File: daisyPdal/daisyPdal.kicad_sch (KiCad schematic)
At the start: 17 parts, among them J1 AudioJack2, U1 L78L05_TO92, U2 TL072

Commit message: Get the input and output buffers on the schematic
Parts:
- added C10, C9: 1u, symbol Device:C
- added J2: AudioJack2, symbol Connector_Audio:AudioJack2
- added R5, R6: 1M, symbol Device:R_US
- added R7: 100K, symbol Device:R_US
- added R8: 100R, symbol Device:R_US
- C6: value C -> 100p
- C7: value C -> 1n
- C8: value C -> 1u
- R1, R2: value R_US -> 1M
- R3: value R_US -> 1k
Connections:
- net +5V: now also R5.1
- net GND: now also A1.20 (AGND), A1.40 (DGND), J2.S, R6.2, R7.2
- net Left in: now also A1.16 (AUDIO_IN_1)
- net VCC: now also A1.39 (VIN)
- net Left out: now reaches A1.18 (AUDIO_OUT_1)
- net Left out: now also C10.1
- net at U2.5 (+): now also C10.2, R5.2, R6.1
- net at U2.6 (-): now also U2.7, R8.1
- new net: C9.1, R8.2
- new net: C9.2, J2.T, R7.1
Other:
- moved on the sheet: U2B

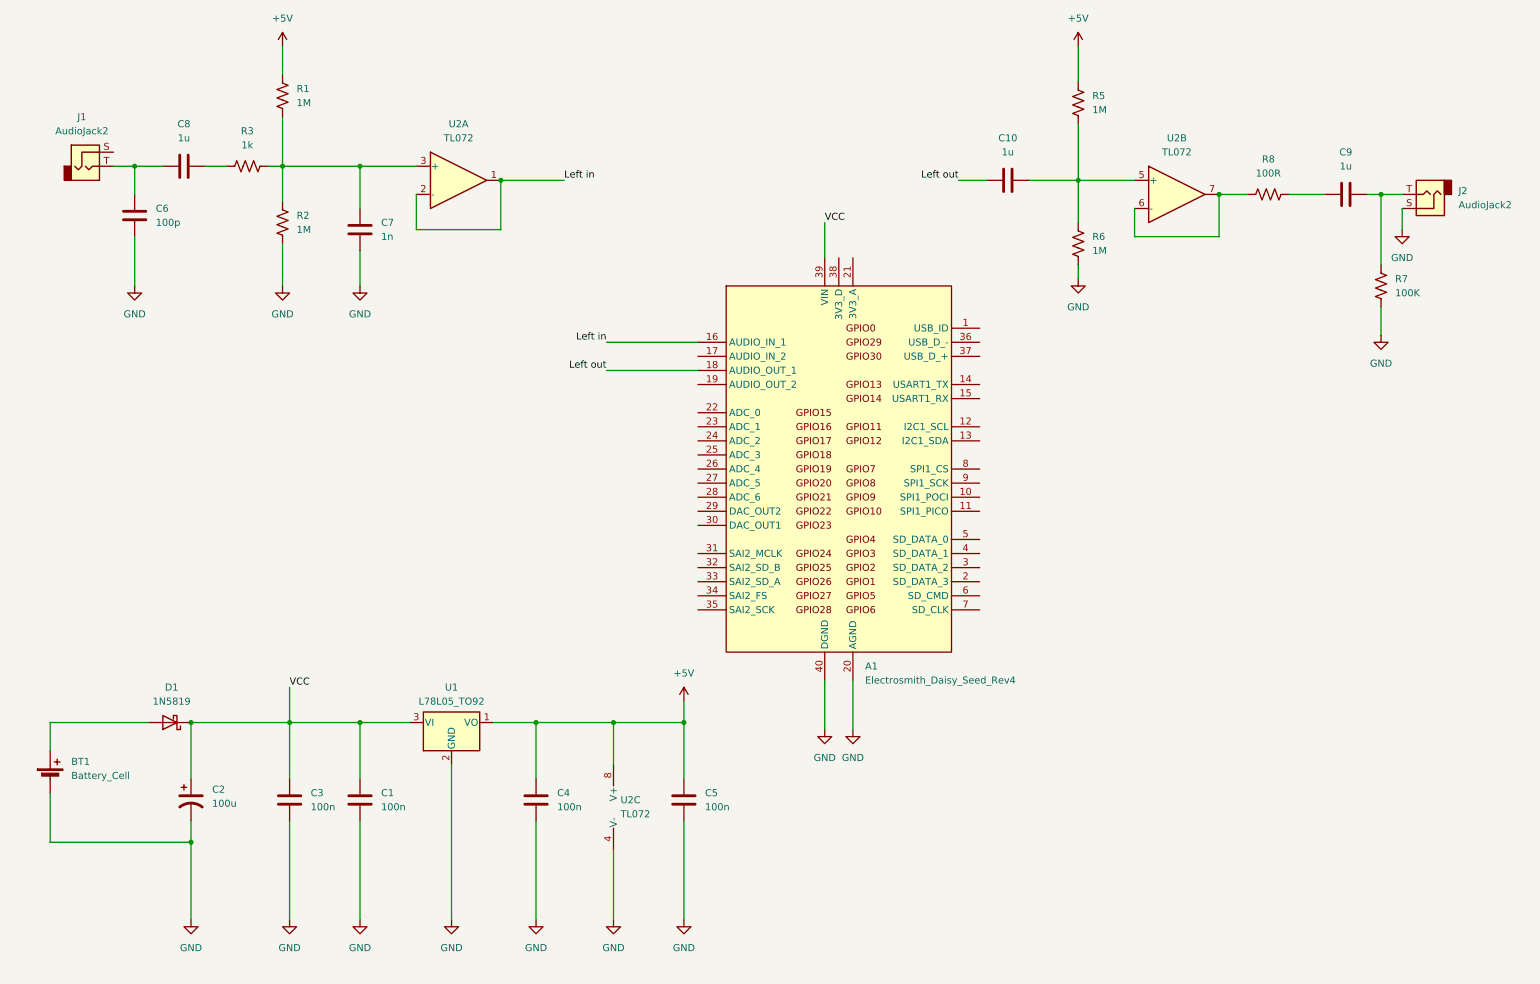
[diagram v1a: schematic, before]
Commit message: Update schematic with pots, switches, encoder, LEDs
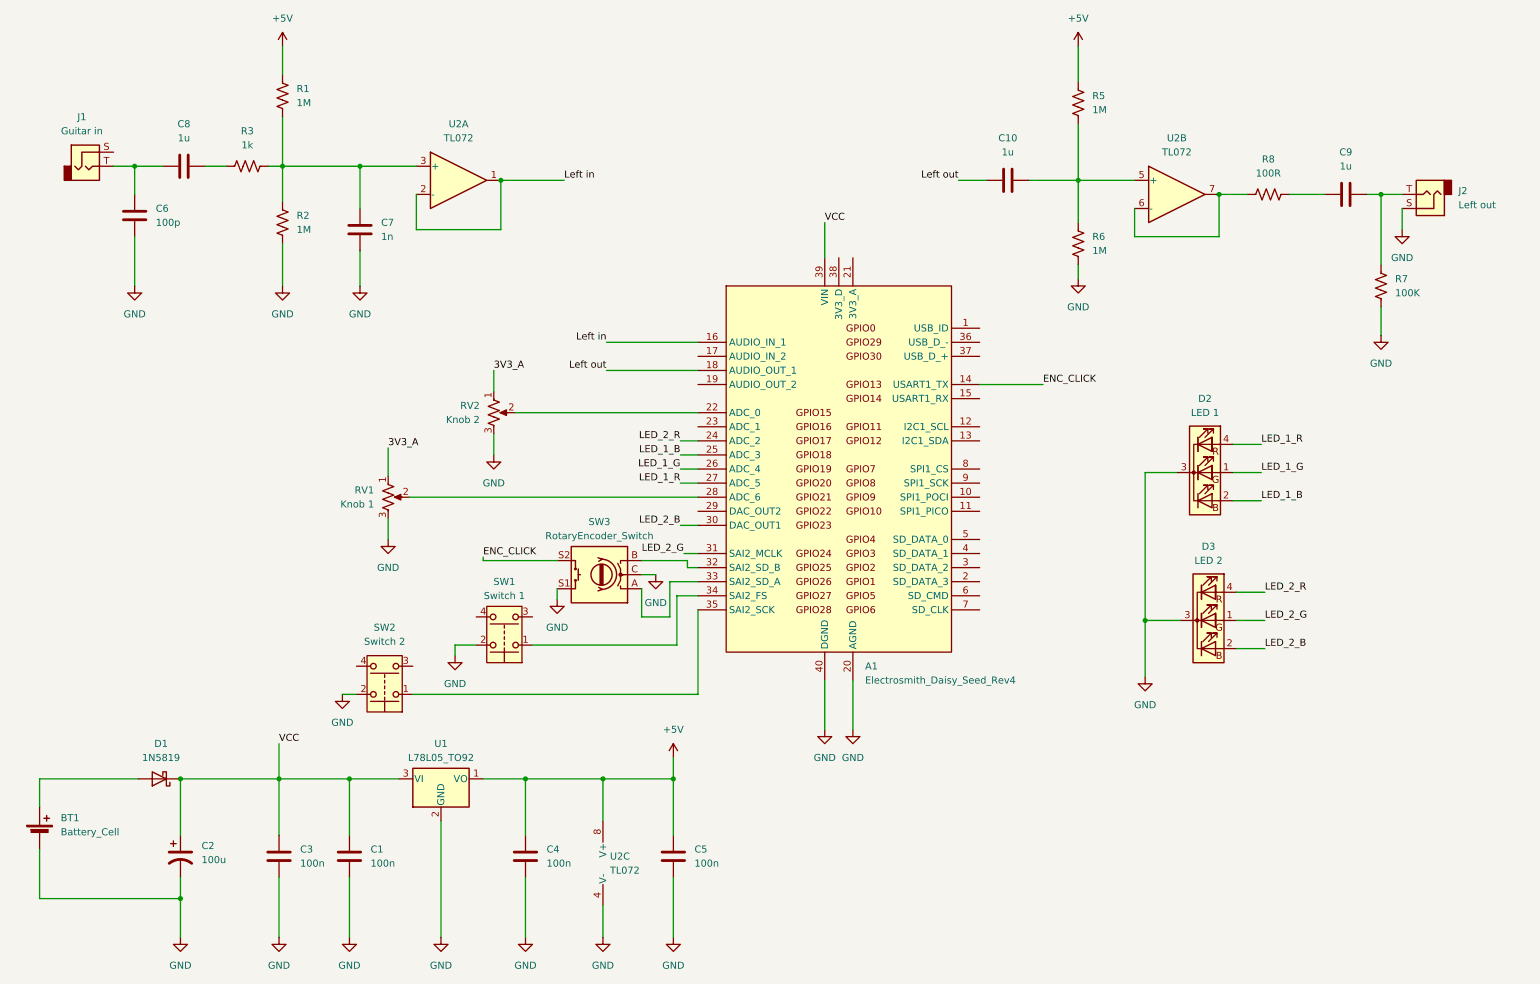
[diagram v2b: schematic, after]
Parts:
- added D2: LED 1, symbol Device:LED_GBKR
- added D3: LED 2, symbol Device:LED_GBKR
- added RV1: Knob 1, symbol Device:R_Potentiometer_US
- added RV2: Knob 2, symbol Device:R_Potentiometer_US
- added SW1: Switch 1, symbol Switch:SW_Push_Dual
- added SW2: Switch 2, symbol Switch:SW_Push_Dual
- added SW3: RotaryEncoder_Switch, symbol Device:RotaryEncoder_Switch
- BT1: footprint (none) -> Jumper:SolderJumper-2_P1.3mm_Open_RoundedPad1.0x1.5mm
- C1, C2, C3, C4, C5, C6: footprint (none) -> Capacitor_THT:CP_Radial_D8.0mm_P3.80mm
- C10, C7, C8, C9: footprint (none) -> Capacitor_THT:C_Rect_L7.0mm_W2.0mm_P5.00mm
- J1: value AudioJack2 -> Guitar in; footprint (none) -> Connector_Audio:Jack_6.35mm_Neutrik_NRJ4HF_Horizontal
- J2: value AudioJack2 -> Left out; footprint (none) -> Connector_Audio:Jack_6.35mm_Neutrik_NRJ4HF_Horizontal
- R1, R2, R3, R5, R6, R7, R8: footprint (none) -> Resistor_THT:R_Box_L13.0mm_W4.0mm_P9.00mm
- U2: footprint (none) -> Package_DIP:DIP-8_W7.62mm_Socket
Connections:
- net GND: now also D2.3 (K), D3.3 (K), RV1.3, RV2.3, SW1.2, SW2.2, SW3.C, SW3.S1
- net ENC_CLICK: now reaches A1.14 (USART1_TX)
- net ENC_CLICK: now also SW3.S2
- net at A1.22 (ADC_0): now also RV2.2
- net LED_2_R: now reaches A1.24 (ADC_2)
- net LED_2_R: now also D3.4 (RA)
- net LED_1_B: now reaches A1.25 (ADC_3)
- net LED_1_B: now also D2.2 (BA)
- net LED_1_G: now reaches A1.26 (ADC_4)
- net LED_1_G: now also D2.1 (GA)
- net LED_1_R: now reaches A1.27 (ADC_5)
- net LED_1_R: now also D2.4 (RA)
- net at A1.28 (ADC_6): now also RV1.2
- net LED_2_B: now reaches A1.30 (DAC_OUT1)
- net LED_2_B: now also D3.2 (BA)
- net LED_2_G: now reaches A1.31 (SAI2_MCLK)
- net LED_2_G: now also D3.1 (GA)
- net at A1.32 (SAI2_SD_B): now also SW3.B
- net at A1.33 (SAI2_SD_A): now also SW3.A
- net at A1.34 (SAI2_FS): now also SW1.1
- net at A1.35 (SAI2_SCK): now also SW2.1
- new net 3V3_A: RV1.1, RV2.1
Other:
- moved on the sheet: BT1, C1, C2, C3, C4, C5, D1, U1, U2C

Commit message: Lots of work on the schematic and PCB
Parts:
- added D4: LED, LED_THT:LED_D1.8mm_W3.3mm_H2.4mm, symbol Device:LED
- added J3: fsw pin 1, Connector_Wire:SolderWire-0.75sqmm_1x01_D1.25mm_OD3.5mm, symbol Connector_Generic:Conn_01x01
- added J4: fsw pin 4, Connector_Wire:SolderWire-0.75sqmm_1x01_D1.25mm_OD3.5mm, symbol Connector_Generic:Conn_01x01
- added J5: fsw pin 6, Connector_Wire:SolderWire-0.75sqmm_1x01_D1.25mm_OD3.5mm, symbol Connector_Generic:Conn_01x01
- added J6: fsw pin 3, Connector_Wire:SolderWire-0.75sqmm_1x01_D1.25mm_OD3.5mm, symbol Connector_Generic:Conn_01x01
- added J7: fsw pin 2, Connector_Wire:SolderWire-0.75sqmm_1x01_D1.25mm_OD3.5mm, symbol Connector_Generic:Conn_01x01
- added J8: fsw pin 5, Connector_Wire:SolderWire-0.75sqmm_1x01_D1.25mm_OD3.5mm, symbol Connector_Generic:Conn_01x01
- added R4: 1k, Resistor_THT:R_Axial_DIN0207_L6.3mm_D2.5mm_P10.16mm_Horizontal, symbol Device:R_US
- BT1: footprint Jumper:SolderJumper-2_P1.3mm_Open_RoundedPad1.0x1.5mm -> Connector_BarrelJack:BarrelJack_Horizontal
- C1, C3, C4, C5, C6: footprint Capacitor_THT:CP_Radial_D8.0mm_P3.80mm -> Capacitor_THT:C_Rect_L9.0mm_W2.5mm_P7.50mm_MKT
- C10, C7, C8, C9: footprint Capacitor_THT:C_Rect_L7.0mm_W2.0mm_P5.00mm -> Capacitor_THT:C_Rect_L9.0mm_W2.5mm_P7.50mm_MKT
- C2: footprint Capacitor_THT:CP_Radial_D8.0mm_P3.80mm -> Capacitor_THT:C_Radial_D10.0mm_H16.0mm_P5.00mm
- D1: footprint Diode_THT:D_DO-41_SOD81_P10.16mm_Horizontal -> Diode_THT:D_DO-41_SOD81_P7.62mm_Horizontal
- D2, D3: footprint (none) -> LED_THT:LED_D5.0mm-4_RGB
- J1, J2: footprint Connector_Audio:Jack_6.35mm_Neutrik_NRJ4HF_Horizontal -> Connector_Audio:Jack_6.35mm_Neutrik_NRJ6HM-1_Horizontal
- R1, R2, R3, R5, R6, R7, R8: footprint Resistor_THT:R_Box_L13.0mm_W4.0mm_P9.00mm -> Resistor_THT:R_Axial_DIN0207_L6.3mm_D2.5mm_P10.16mm_Horizontal
- RV1, RV2: footprint (none) -> Potentiometer_THT:Potentiometer_Alps_RK09K_Single_Vertical
- SW1, SW2: footprint (none) -> Button_Switch_THT:SW_CW_GPTS203211B_1 podal
- SW3: footprint (none) -> Rotary_Encoder:RotaryEncoder_Alps_EC12E-Switch_Vertical_H20mm
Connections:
- net 3V3_A is gone; now on net 3v3: RV1.1, RV2.1
- net GND: now also J1.S, J8.1 (Pin_1)
- net at BT1.1 (+), D1.2 (A): now also R4.1
- net at C6.1, C8.1: now also J4.1 (Pin_1); no longer J1.T
- net 3v3: now reaches A1.21 (3V3_A)
- net at C9.2, R7.1: now also J6.1 (Pin_1); no longer J2.T
- new net: J1.T, J3.1 (Pin_1)
- new net: D4.1 (K), J7.1 (Pin_1)
- new net: D4.2 (A), R4.2
- new net: J2.T, J5.1 (Pin_1)
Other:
- moved on the sheet: C10, C6, C7, C8, J1, J2, R1, R2, R3, U2A

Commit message: Replace u1 footprint to get correct spacing
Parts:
- U1: footprint Package_TO_SOT_THT:TO-92_Inline -> Package_TO_SOT_THT:TO-92_Inline_Wide
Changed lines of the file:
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@@
       (effects (font (size 1.27 1.27)))
     )
-    (property "Footprint" "Package_TO_SOT_THT:TO-92_Inline" (at 90.805 155.575 0)
+    (property "Footprint" "Package_TO_SOT_THT:TO-92_Inline_Wide" (at 90.805 155.575 0)
       (effects (font (size 1.27 1.27) italic) hide)
     )
